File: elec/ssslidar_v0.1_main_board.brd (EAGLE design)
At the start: 30 x 41 mm, 79 parts, among them IC1 MIC5504-2.8YM5, IC2 MIC5504-2.8YM5, K1 BUTTON-2P-REINFORCE-3100060P1, P1 PIN_SMD_0.8X1.6, P10 PIN_SMD_0.8X1.6, P11 PIN_SMD_0.8X1.6, P12 PIN_SMD_0.8X1.6, P13 PIN_SMD_0.8X1.6, P14 PIN_SMD_0.8X1.6, P15 PIN_SMD_0.8X1.6, P16 PIN_SMD_0.8X1.6, P17 PIN_SMD_0.8X1.6, P18 PIN_SMD_0.8X1.6, P19 PIN_SMD_0.8X1.6, P2 PIN_SMD_0.8X1.6, P20 PIN_SMD_0.8X1.6, P21 PIN_SMD_0.8X1.6, P22 PIN_SMD_0.8X1.6, P23 PIN_SMD_0.8X1.6, P24 PIN_SMD_0.8X1.6, P25 PIN_SMD_0.8X1.6, P26 PIN_SMD_0.8X1.6, P27 PIN_SMD_0.8X1.6, P28 PIN_SMD_0.8X1.6, P3 PIN_SMD_1X1, P4 PIN_SMD_0.8X1.6, P5 PIN_SMD_0.8X1.6, P6 PIN_SMD_1X1, P7 PIN_SMD_1X1, P8 PIN_SMD_1X1, P9 PIN_SMD_0.8X1.6, Q1 XRCGB24M000F3M00R0 (24MHz), U1 VL53L0X, U2 TPS62173DSG, U4 STM32F301K6U6

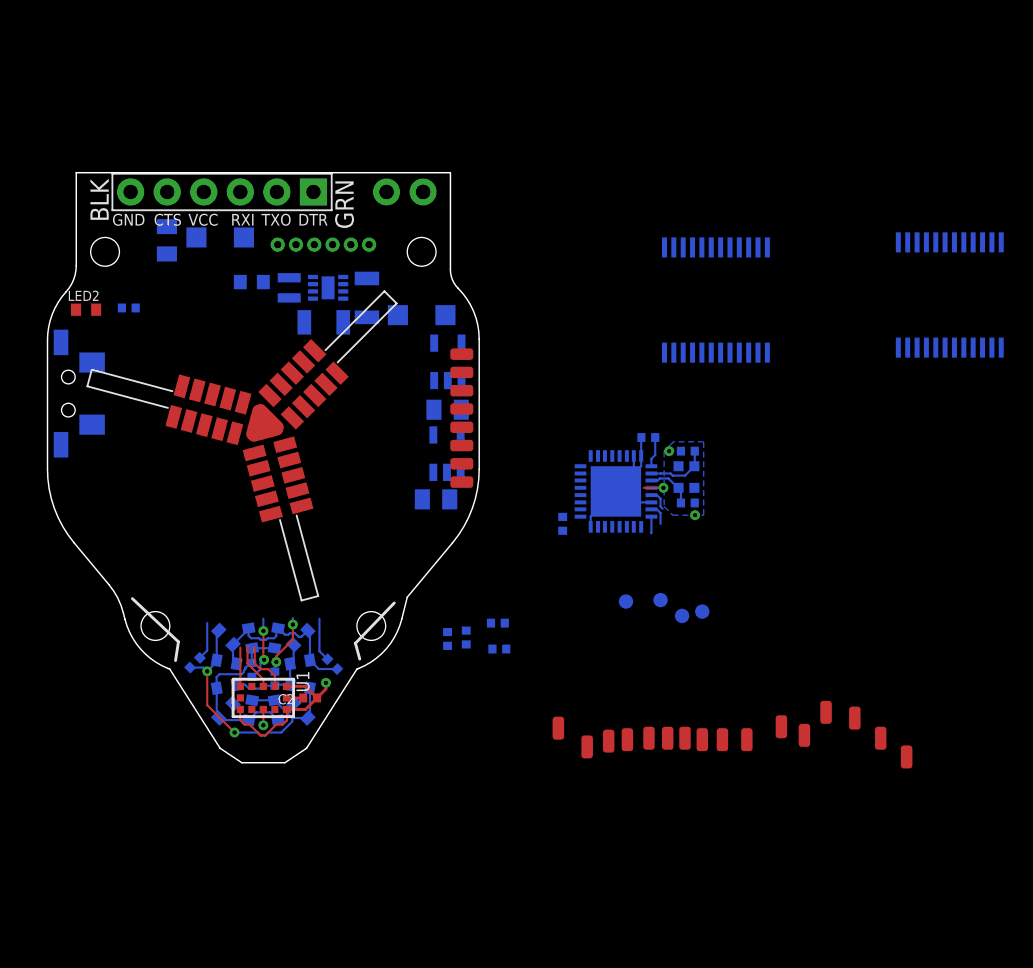
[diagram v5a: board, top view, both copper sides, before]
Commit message: Routed blades
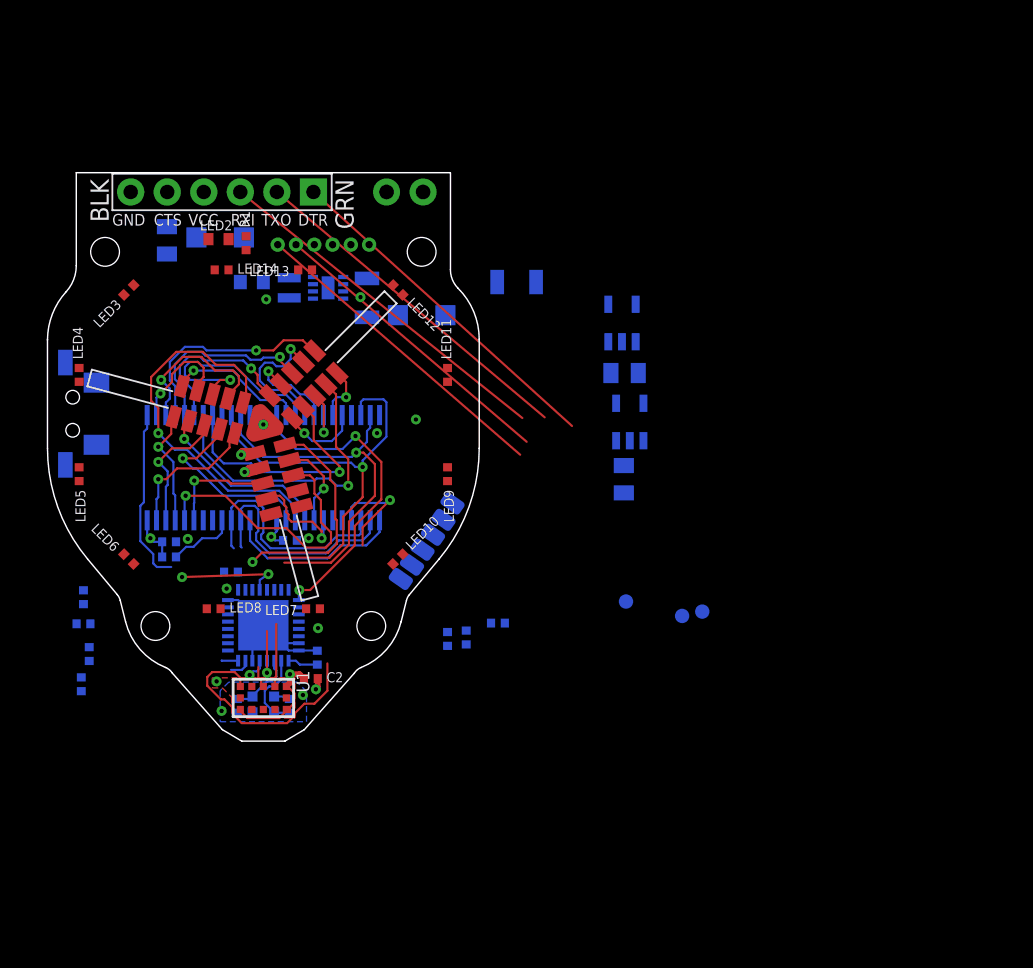
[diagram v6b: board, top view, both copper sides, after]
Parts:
- removed P1, P13, P16, P17, P18, P19, P20, P21, P22, P23, P24, P25, P26, P27, P28, P4, P5, P9: PIN_SMD_0.8X1.6, Xevelabs:PIN_SMD_0.8X1.6
- removed P8: PIN_SMD_1X1, Xevelabs:PIN_SMD_1X1
- added C1, C5: 100nF, Xevelabs:0402_N
- LED10, LED11, LED12, LED13, LED14, LED3, LED4, LED5, LED6, LED7, LED8, LED9: device Xevelabs:D_0603_L -> Xevelabs:D_0402_N
- P10, P11, P12, P14, P15, P2: value PIN_SMD_0.8X1.6 -> PIN_SMD_1X1.6; device Xevelabs:PIN_SMD_0.8X1.6 -> Xevelabs:PIN_SMD_1X1.6
- moved U$1 53.6 mm to (10.5, 20.5)
- moved C9 34.3 mm to (13.2, 3.95), turned to 270 degrees
- moved Q1 33.4 mm to (15.0, 4.05), turned to 0 degrees
- moved C10 32.9 mm to (16.8, 3.95), turned to 90 degrees
- moved U$2 29.4 mm to (19.5, 20.5)
- moved C14 27.6 mm to (18.8, 7.30), turned to 90 degrees
- moved LED12 26.9 mm to (24.4, 32.9), flipped to the top, turned to 315 degrees
- moved LED3 26.9 mm to (5.65, 32.9), flipped to the top, turned to 225 degrees
- moved U4 26.2 mm to (15.0, 9.55), turned to 90 degrees
- moved LED13 25.9 mm to (17.9, 34.2), flipped to the top, turned to 180 degrees
- moved LED14 25.9 mm to (12.1, 34.2), flipped to the top, turned to 0 degrees
- moved LED11 25.2 mm to (27.8, 26.9), flipped to the top, turned to 90 degrees
- moved LED4 25.2 mm to (2.20, 26.9), flipped to the top, turned to 90 degrees
- moved R3 23.8 mm to (8.45, 14.3), turned to 0 degrees
- moved C13 23.3 mm to (12.8, 13.2), turned to 0 degrees
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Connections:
- net N$7 renamed 5V_OUT
- removed net DBG_GPIO4: P8.P$1, U4.28
- net A_INT1: now also U$2.19; no longer U$2.9
- net A_INT2: now also U$2.20; no longer U$2.8
- net A_SDA1: now also U$1.19; no longer U$1.9
- net A_SDA2: now also U$1.20; no longer U$1.8
- net B_INT2: now also U$2.4; no longer U$2.6
- net B_SDA2: now also U$1.4; no longer U$1.6
- net C_INT1: now also U$2.2; no longer U$2.5
- net C_INT2: now also U$2.21; no longer U$2.4
- net C_SDA1: now also U$1.2; no longer U$1.5
- net C_SDA2: now also U$1.21; no longer U$1.4
- net DBG_GPIO1: no longer U4.21
- net DBG_GPIO2: no longer U4.22
- net DBG_GPIO3: no longer U4.18
- net D_INT1: now also U$2.23; no longer U$2.3
- net D_INT2: now also U$2.8; no longer U$2.2
- net D_SDA1: now also U$1.23; no longer U$1.3
- net D_SDA2: now also U$1.8; no longer U$1.2
- net E_INT1: now also U$2.6; no longer U$2.23
- net E_INT2: now also U$2.5; no longer U$2.22
- net E_SDA1: now also U$1.6; no longer U$1.23
- net E_SDA2: now also U$1.5; no longer U$1.22
- net F_INT1: now also U$2.3; no longer U$2.21
- net F_INT2: now also U$2.22; no longer U$2.20
- net F_SDA1: now also U$1.3; no longer U$1.21
- net F_SDA2: now also U$1.22; no longer U$1.20
- net GND: now also C1.2, C5.2
- net G_INT1: now also U$2.16; no longer U$2.19
- net G_SDA1: now also U$1.16; no longer U$1.19
- net RXD: no longer P5.PIN
- net TXD: no longer P4.PIN
- net VDD: now also C1.1, C5.1, R3.2
- net VEE: no longer R3.2
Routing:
- net MUX_ADDR0: track 0.00 -> 30.8 mm, vias 0 -> 1
- net F_INT2: track 0.00 -> 26.6 mm, vias 0 -> 1
- net MUX_ADDR1: track 0.00 -> 26.1 mm, vias 0 -> 1
- net RXD: track 0.00 -> 25.1 mm
- net TXD: track 0.00 -> 24.3 mm
- net DTR: track 0.00 -> 24.2 mm
- net INT: track 0.00 -> 22.4 mm, vias 0 -> 2
- net DXL>MCU: track 0.00 -> 22.3 mm
- net G_INT1: track 2.70 -> 24.2 mm, vias 0 -> 1
- net B_SDA1: track 0.00 -> 21.4 mm, vias 0 -> 1
- net DXL<MCU: track 0.00 -> 21.1 mm
- net N$11: track 20.8 -> 0.00 mm, vias 2 -> 0
- net A_SDA2: track 0.00 -> 19.9 mm, vias 0 -> 1
- net SDA: track 0.00 -> 19.6 mm, vias 0 -> 2
- net D_SDA2: track 0.00 -> 17.6 mm, vias 0 -> 1
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- added copper zone on layer 3, net 5V_OUT
- added copper zone on layer 2, net N$7
- added copper zone on layer 3, net VEE
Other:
- board size 30 x 41 mm -> 30 x 39.5 mm
- board text added: "S"

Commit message: LEDs routed. Mostly power left to route.
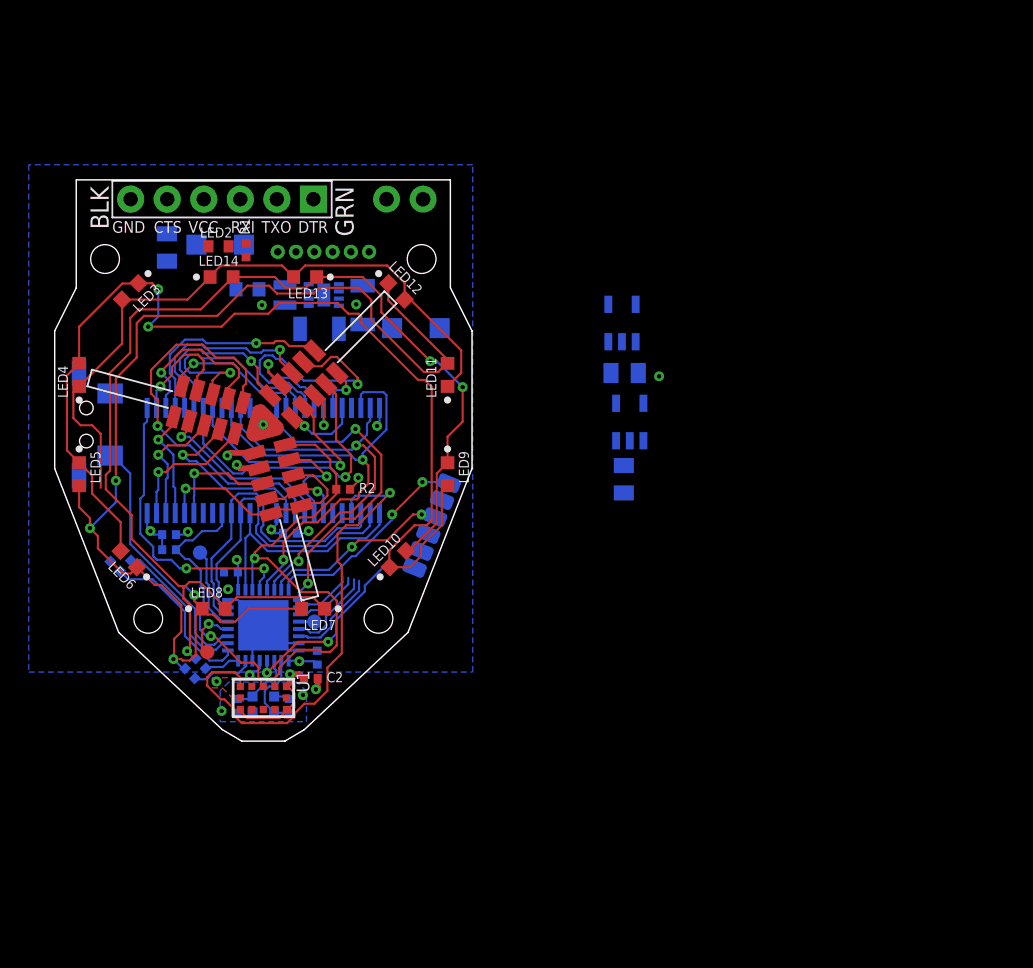
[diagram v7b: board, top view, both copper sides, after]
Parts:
- removed C8: 100nF, Xevelabs:0402_N
- removed R4: 10k, Xevelabs:0402_N
- LED10, LED11, LED12, LED13, LED14, LED3, LED4, LED5, LED6, LED7, LED8, LED9: device Xevelabs:D_0402_N -> Xevelabs:D_0603_N
- moved P6 33.1 mm to (11.1, 7.70), flipped to the top
- moved P7 29.8 mm to (10.6, 14.6)
- moved P3 27.0 mm to (18.6, 9.80)
- moved R2 14.2 mm to (20.6, 19.0), flipped to the top, turned to 0 degrees
- moved C11 14.1 mm to (18.9, 30.1)
- moved R8 9.10 mm to (9.90, 6.20), turned to 45 degrees
- moved R9 8.60 mm to (10.7, 6.90), turned to 45 degrees
- moved R5 8.53 mm to (4.70, 13.7), turned to 45 degrees
- moved R7 7.31 mm to (5.45, 14.4), turned to 45 degrees
- moved P11 1.42 mm to (27.9, 19.4), turned to 22 degrees
- moved P15 1.37 mm to (27.4, 18.2), turned to 22 degrees
- moved P12 1.24 mm to (26.9, 17.1), turned to 22 degrees
- moved P10 1.23 mm to (25.5, 13.5), turned to 22 degrees
- moved K1 1.21 mm to (2.70, 23.5)
- moved P2 1.16 mm to (26.5, 15.9), turned to 22 degrees
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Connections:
- removed net DTR: C8.1, JP1.P$1
- net !MUX_EN: now also U4.14; no longer U4.15
- net A_INT1: now also B1.8
- net A_SDA2: now also B1.6, B1.7
- net COM_RST: no longer C8.2, R4.2
- net DBG_GPIO1: now also U4.28
- net DBG_GPIO2: now also U4.13
- net DBG_GPIO3: now also U4.12
- net LED1: now also U4.9; no longer U4.7
- net LED2: now also U4.10; no longer U4.8
- net LED3: now also U4.7; no longer U4.9
- net LED4: now also U4.8; no longer U4.10
- net MUX_ADDR0: now also U4.21; no longer U4.11
- net MUX_ADDR1: now also U4.22; no longer U4.12
- net MUX_ADDR2: now also U4.15; no longer U4.13
- net MUX_ADDR3: now also U4.18; no longer U4.14
- net N$4: now also U4.11
- net VDD: no longer R4.1
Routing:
- net N$11: track 0.00 -> 81.9 mm, vias 0 -> 4
- net N$12: track 0.00 -> 80.8 mm, vias 0 -> 3
- net N$10: track 0.00 -> 72.8 mm, vias 0 -> 2
- net N$9: track 0.00 -> 47.0 mm
- net DTR: track 24.2 -> 0.00 mm
- net RXD: track 25.1 -> 6.59 mm
- net TXD: track 24.3 -> 6.20 mm
- net N$4: track 0.00 -> 17.8 mm
- net DXL>MCU: track 22.3 -> 4.75 mm
- net DXL<MCU: track 21.1 -> 4.16 mm
- net SWCLK: track 0.00 -> 14.9 mm, vias 0 -> 2
- net SWDIO: track 0.00 -> 13.3 mm, vias 0 -> 2
- net SCL: track 19.9 -> 32.3 mm
- net G_SDA1: track 6.25 -> 18.0 mm, vias 0 -> 1
- net G_INT1: track 24.2 -> 34.6 mm
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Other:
- board size 30 x 39.5 mm -> 29 x 39 mm
- board text removed: "S"

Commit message: Only power and cosmetics left
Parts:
- added R4, R6: TBD, Xevelabs:0402_N
- moved C6 37.8 mm to (2.43, 29.6), turned to 90 degrees
- moved IC1 34.0 mm to (5.90, 29.8), turned to 90 degrees
- moved IC2 13.9 mm to (27.2, 28.1), turned to 180 degrees
- moved C4 13.9 mm to (27.2, 25.0), turned to 180 degrees
- moved D1 1.98 mm to (24.2, 28.8), turned to 270 degrees
- moved LED2 1.13 mm to (10.8, 36.0), turned to 180 degrees
- moved R1 0.94 mm to (12.9, 36.0), turned to 0 degrees
- moved R3 0.55 mm to (9.00, 14.8)
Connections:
- new net N$13: JP1.P$2, R4.2
- new net N$14: JP1.P$3, R6.2
- new net N$15: IC2.4
- net RXD: now also R6.1; no longer JP1.P$3
- net TXD: now also R4.1; no longer JP1.P$2
- net VDD: no longer R3.2
- net VEE: now also R3.2
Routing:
- net VEE: track 9.63 -> 48.7 mm, vias 3 -> 4
- net N$11: track 81.9 -> 63.9 mm, vias 4 -> 3
- net DXL>MCU: track 4.75 -> 18.9 mm
- net DXL<MCU: track 4.16 -> 17.9 mm
- net RXD: track 6.59 -> 15.9 mm
- net N$10: track 72.8 -> 63.7 mm, vias 2 -> 3
- net TXD: track 6.20 -> 15.1 mm
- net N$14: track 0.00 -> 8.16 mm, vias 0 -> 1
- net N$13: track 0.00 -> 7.89 mm, vias 0 -> 1
- net N$9: track 47.0 -> 54.3 mm, vias 0 -> 1
- net N$12: track 80.8 -> 75.6 mm
- net +12V: track 0.00 -> 4.16 mm
- net MUX_ADDR0: track 32.8 -> 28.9 mm, vias 2 -> 3
- net 5V_OUT: track 0.00 -> 3.48 mm, vias 1 -> 2
- net COM_RST: track 13.3 -> 16.4 mm
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- removed copper zone on layer 3, net VEE
